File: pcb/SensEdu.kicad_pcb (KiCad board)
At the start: 4 copper layers, 99.1 x 54 mm, 147 parts, among them J1 Power, J10 Barrel_Jack_Switch, J11 Conn_01x04_Pin, J12 Conn_01x04_Pin, J13 Conn_02x01, J14 Conn_02x01, J15 Conn_02x01, J16 Conn_02x01, J19 Conn_03x01, J2 PWM, J20 Conn_01x04_Pin, J3 Analog, J4 PWM, J5 Analog, J6 Communication, J7 Digital, J9 Conn_01x04_Pin, U1 AD8426ACPZ-R7, U12 TLS850C2TE_V33, U13 NCP1117-2.5_SOT223, U2 AD8426ACPZ-R7, U3 LT1790ACS6-1.25, U4 ADA4891, U5 AD8426ACPZ-R7, U6 AD8426ACPZ-R7, U7 ADA4891, U8 DPS310XTSA1

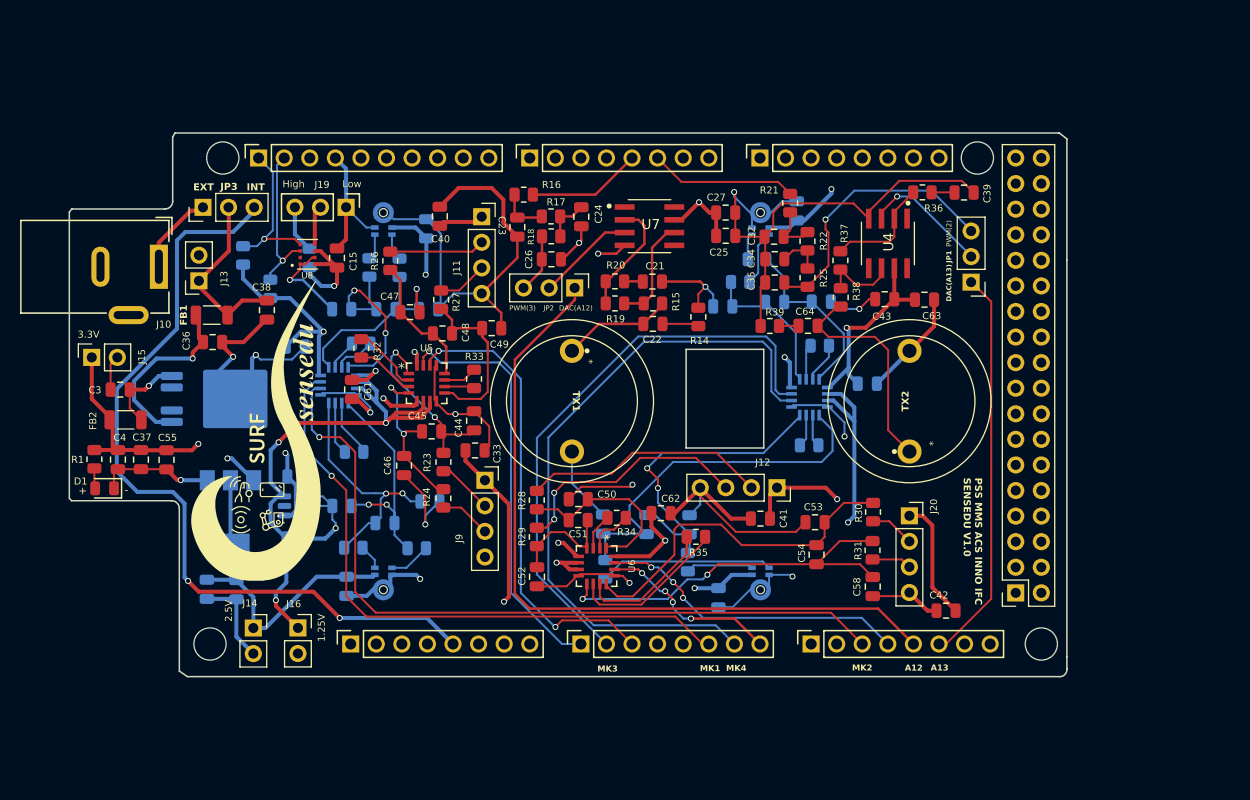
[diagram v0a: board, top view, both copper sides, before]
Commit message: pcb: New PCB revision (#88)
- Rearrange schematics
- Better symbols and footprints
- Better names and graphics
- Add simulations for DC offset after AC coupling
- Add BOM
- Redraw PCB layout
- Proper position for pressure and humidity sensor
- Better positions for EXT headers
- Silkscreen text labels for headers, pins, mics, etc.
- Change supply polarity and pin numbers of ADA4511
- Change cap of switches to 100n to reduce BOM
- Change supply of sensors to unison 3.3V
- Rearrange ADC pins
- Add digital switches instead of manual headers
- Add logos

---------

Co-authored-by: oberfeli <felix.ober@mailbox.org>
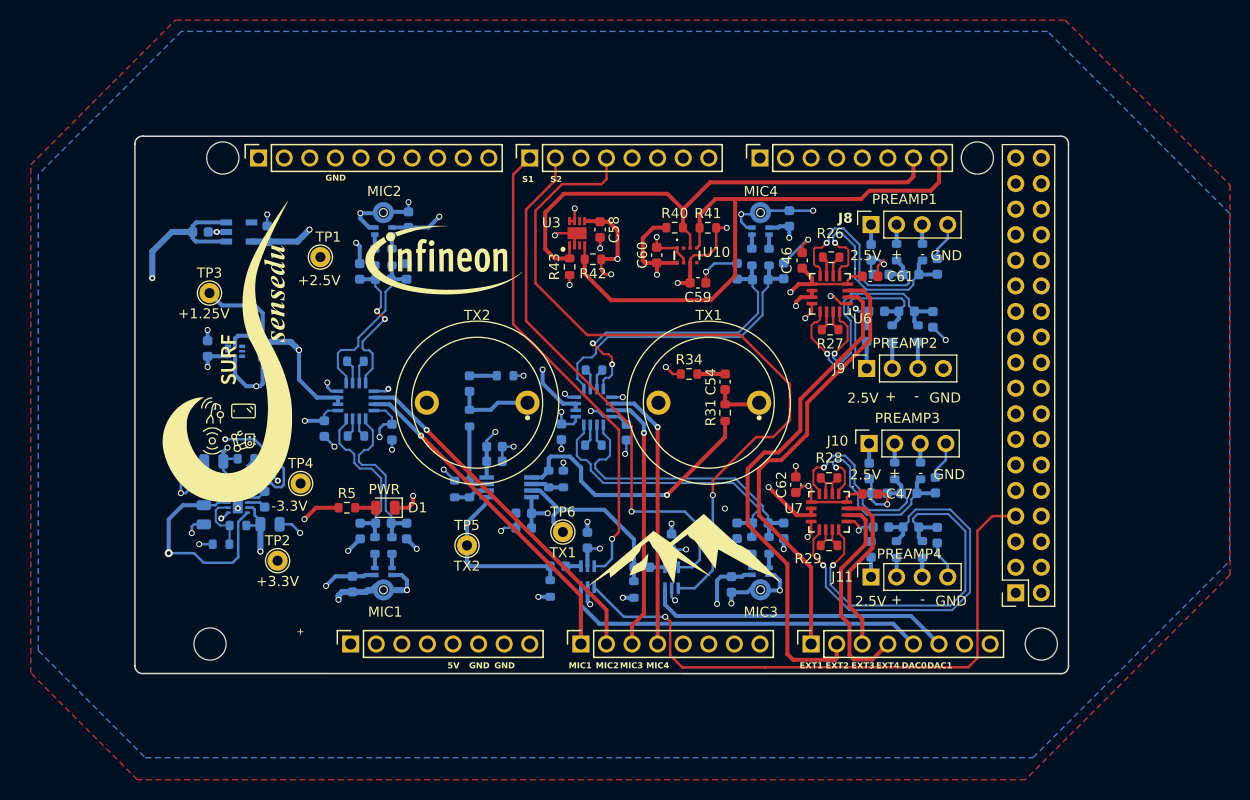
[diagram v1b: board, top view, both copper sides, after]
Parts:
- removed C63: 100n, Capacitor_SMD:C_0805_2012Metric
- removed C64: DNI, Capacitor_SMD:C_0805_2012Metric
- removed FB1, FB2: FerriteBead, Inductor_SMD:L_1206_3216Metric
- removed the G*** at (118.5, 76.2)
- removed J12, J20: Conn_01x04_Pin, Connector_PinSocket_2.54mm:PinSocket_1x04_P2.54mm_Vertical
- removed J13, J14, J15, J16: Conn_02x01, Connector_PinSocket_2.54mm:PinSocket_1x02_P2.54mm_Vertical
- removed J19: Conn_03x01, Connector_PinHeader_2.54mm:PinHeader_1x03_P2.54mm_Vertical
- removed the J9 at (141.3, 81.2)
- removed JP1, JP2, JP3: Jumper_3_Bridged12, Connector_PinHeader_2.54mm:PinHeader_1x03_P2.54mm_Vertical
- removed LS1, LS2: 328ST16M, SensEdu:328ST16M_Speaker
- removed U12: TLS850C2TE_V33, Package_TO_SOT_SMD:TO-252-4
- added C19: 100p, Capacitor_SMD:C_0603_1608Metric, B.Cu at (133.5, 60.5)
- added C59: 100n, Capacitor_SMD:C_0603_1608Metric, F.Cu at (162.4, 61.6)
- added C60: 100n, Capacitor_SMD:C_0603_1608Metric, F.Cu at (158.3, 58.8)
- added G***: LOGO, LOGO, F.Cu at (137.4, 59.4)
- added G***: LOGO, SensEdu:logo2, F.Cu at (115.7, 68.4)
- added G***: LOGO, LOGO, F.Cu at (161.1, 87.9)
- added J11: Conn_01x04_Pin, Connector_PinSocket_2.54mm:PinSocket_1x04_P2.54mm_Vertical, F.Cu at (179.6, 90.8)
- added J8: Conn_01x04_Pin, Connector_PinSocket_2.54mm:PinSocket_1x04_P2.54mm_Vertical, F.Cu at (179.6, 55.8)
- added R43: 10k, Resistor_SMD:R_0603_1608Metric, F.Cu at (149.7, 60.0)
- added TP1: +2.5V, TestPoint:TestPoint_THTPad_D2.0mm_Drill1.0mm, F.Cu at (124.9, 59.0)
- added TP2: +3.3V, TestPoint:TestPoint_THTPad_D2.0mm_Drill1.0mm, F.Cu at (120.7, 89.2)
- added TP3: +1.25V, TestPoint:TestPoint_THTPad_D2.0mm_Drill1.0mm, F.Cu at (113.9, 62.6)
- added TP4: -3.3V, TestPoint:TestPoint_THTPad_D2.0mm_Drill1.0mm, F.Cu at (123.0, 81.5)
- added TP5: TX2, TestPoint:TestPoint_THTPad_D2.0mm_Drill1.0mm, F.Cu at (139.5, 87.7)
- added TP6: TX1, TestPoint:TestPoint_THTPad_D2.0mm_Drill1.0mm, F.Cu at (149.0, 86.3)
- added TX1: 328ST16M, SensEdu:328ST16M_Speaker, F.Cu at (163.5, 73.5)
- added TX2: 328ST16M, SensEdu:328ST16M_Speaker, F.Cu at (140.5, 73.5)
- added U10: DPS368XTSA1, SensEdu:DPS368XTSA1, F.Cu at (161.3, 58.9)
- added U11: ADA4511-2ARMZ, SamacSys_Parts:SOP65P490X110-8N, B.Cu at (143.7, 81.9)
- added U9: NC7SB3157P6X, SensEdu:SOT65P210X110-6N, B.Cu at (151.5, 90.8)
- C1, C10, C11, C2: value 100n -> 1u; footprint Capacitor_SMD:C_0805_2012Metric -> Capacitor_SMD:C_0603_1608Metric
- C12, C13: value 470p -> 100n; footprint Capacitor_SMD:C_0805_2012Metric -> Capacitor_SMD:C_0603_1608Metric
- C14: value 1u -> 470p; footprint Capacitor_SMD:C_0805_2012Metric -> Capacitor_SMD:C_0603_1608Metric
- C15, C36: value 100n -> 470p; footprint Capacitor_SMD:C_0805_2012Metric -> Capacitor_SMD:C_0603_1608Metric; moved to B.Cu
- C16, C18, C57, C61, C62: footprint Capacitor_SMD:C_0805_2012Metric -> Capacitor_SMD:C_0603_1608Metric
- C17: value 470p -> 100p; footprint Capacitor_SMD:C_0805_2012Metric -> Capacitor_SMD:C_0603_1608Metric
- C20: value 1u -> 100n; footprint Capacitor_SMD:C_0805_2012Metric -> Capacitor_SMD:C_0603_1608Metric
- C21, C33, C44: footprint Capacitor_SMD:C_0805_2012Metric -> Capacitor_SMD:C_0603_1608Metric; moved to B.Cu
- C22: value DNI -> 470p; footprint Capacitor_SMD:C_0805_2012Metric -> Capacitor_SMD:C_0603_1608Metric; moved to B.Cu
- C23, C34, C35: value 1n -> 470p; footprint Capacitor_SMD:C_0805_2012Metric -> Capacitor_SMD:C_0603_1608Metric; moved to B.Cu
- C24, C26: value 1n -> 100p; footprint Capacitor_SMD:C_0805_2012Metric -> Capacitor_SMD:C_0603_1608Metric; moved to B.Cu
- C25, C39, C40, C41, C42: value 100n -> 100p; footprint Capacitor_SMD:C_0805_2012Metric -> Capacitor_SMD:C_0603_1608Metric; moved to B.Cu
- C27, C43: value 1u -> 100p; footprint Capacitor_SMD:C_0805_2012Metric -> Capacitor_SMD:C_0603_1608Metric; moved to B.Cu
- C28, C29, C46, C47: value 100p -> 1u; footprint Capacitor_SMD:C_0805_2012Metric -> Capacitor_SMD:C_0603_1608Metric
- C3: value 10u -> 1u; footprint Capacitor_SMD:C_0805_2012Metric -> Capacitor_SMD:C_0603_1608Metric; moved to B.Cu
- C30, C31, C58: value 100p -> 100n; footprint Capacitor_SMD:C_0805_2012Metric -> Capacitor_SMD:C_0603_1608Metric
- C32: value 1n -> 100n; footprint Capacitor_SMD:C_0805_2012Metric -> Capacitor_SMD:C_0603_1608Metric; moved to B.Cu
- C37: value 10u -> 470p; footprint Capacitor_SMD:C_0805_2012Metric -> Capacitor_SMD:C_0603_1608Metric; moved to B.Cu
- C38: value 10u -> 100p; footprint Capacitor_SMD:C_0805_2012Metric -> Capacitor_SMD:C_0603_1608Metric; moved to B.Cu
- C4: value 100n -> 1u; footprint Capacitor_SMD:C_0805_2012Metric -> Capacitor_SMD:C_0603_1608Metric; moved to B.Cu
- C45: value 470p -> 100p; footprint Capacitor_SMD:C_0805_2012Metric -> Capacitor_SMD:C_0603_1608Metric; moved to B.Cu
- C48, C51: value 470p -> 100n; footprint Capacitor_SMD:C_0805_2012Metric -> Capacitor_SMD:C_0603_1608Metric; moved to B.Cu
- C49, C52: value 100p -> 1u; footprint Capacitor_SMD:C_0805_2012Metric -> Capacitor_SMD:C_0603_1608Metric; moved to B.Cu
- C5: value 100p -> 4.7u
- C50, C53: value 100p -> 100n; footprint Capacitor_SMD:C_0805_2012Metric -> Capacitor_SMD:C_0603_1608Metric; moved to B.Cu
- C54: value 470p -> DNI; footprint Capacitor_SMD:C_0805_2012Metric -> Capacitor_SMD:C_0603_1608Metric
- C55: value 100n -> DNI; footprint Capacitor_SMD:C_0805_2012Metric -> Capacitor_SMD:C_0603_1608Metric; moved to B.Cu
- C56: value 10u -> 100n; footprint Capacitor_SMD:C_0805_2012Metric -> Capacitor_SMD:C_0603_1608Metric
- C6: value 470p -> 4.7u
- C7: value 1u -> 2.2u
- C8: value 100n -> 470n; footprint Capacitor_SMD:C_0805_2012Metric -> Capacitor_SMD:C_0603_1608Metric
- C9: value 100p -> 2.2u
- J10: value Barrel_Jack_Switch -> Conn_01x04_Pin; footprint Connector_BarrelJack:BarrelJack_Wuerth_6941xx301002 -> Connector_PinSocket_2.54mm:PinSocket_1x04_P2.54mm_Vertical
- R1: value 47 -> 130k; footprint Resistor_SMD:R_0805_2012Metric -> Resistor_SMD:R_0603_1608Metric; moved to B.Cu
- R10, R11, R6, R8, R9: footprint Resistor_SMD:R_0805_2012Metric -> Resistor_SMD:R_0603_1608Metric
- R12, R13, R7: value 1k -> 3.9k; footprint Resistor_SMD:R_0805_2012Metric -> Resistor_SMD:R_0603_1608Metric
- R14: value DNI -> 1k; footprint Resistor_SMD:R_0805_2012Metric -> Resistor_SMD:R_0603_1608Metric; moved to B.Cu
- R15: value 0 -> 1k; footprint Resistor_SMD:R_0805_2012Metric -> Resistor_SMD:R_0603_1608Metric; moved to B.Cu
- R16, R17: value 4.7k -> 1k; footprint Resistor_SMD:R_0805_2012Metric -> Resistor_SMD:R_0603_1608Metric; moved to B.Cu
- R18, R21, R22, R25: value 4.7k -> 3.9k; footprint Resistor_SMD:R_0805_2012Metric -> Resistor_SMD:R_0603_1608Metric; moved to B.Cu
- R19: value 3k -> 3.9k; footprint Resistor_SMD:R_0805_2012Metric -> Resistor_SMD:R_0603_1608Metric; moved to B.Cu
- R2: value 1k -> 75k; footprint Resistor_SMD:R_0805_2012Metric -> Resistor_SMD:R_0603_1608Metric
- R20: value 1k -> 3.9k; footprint Resistor_SMD:R_0805_2012Metric -> Resistor_SMD:R_0603_1608Metric; moved to B.Cu
- R23, R24: footprint Resistor_SMD:R_0805_2012Metric -> Resistor_SMD:R_0603_1608Metric; moved to B.Cu
- R26, R27, R28, R29: value 3.9k -> 1k; footprint Resistor_SMD:R_0805_2012Metric -> Resistor_SMD:R_0603_1608Metric
- R3: value 3.9k -> 130k; footprint Resistor_SMD:R_0805_2012Metric -> Resistor_SMD:R_0603_1608Metric
- R30: value 3.9k -> 1.2k; footprint Resistor_SMD:R_0805_2012Metric -> Resistor_SMD:R_0603_1608Metric; moved to B.Cu
- R31: value 3.9k -> 0; footprint Resistor_SMD:R_0805_2012Metric -> Resistor_SMD:R_0603_1608Metric
- R32, R33, R36: value 1k -> 22k; footprint Resistor_SMD:R_0805_2012Metric -> Resistor_SMD:R_0603_1608Metric; moved to B.Cu
- R34: value 1k -> DNI; footprint Resistor_SMD:R_0805_2012Metric -> Resistor_SMD:R_0603_1608Metric
- R35: value 1k -> 0; footprint Resistor_SMD:R_0805_2012Metric -> Resistor_SMD:R_0603_1608Metric; moved to B.Cu
- R37: value 3k -> DNI; footprint Resistor_SMD:R_0805_2012Metric -> Resistor_SMD:R_0603_1608Metric; moved to B.Cu
- R38: value 0 -> 22k; footprint Resistor_SMD:R_0805_2012Metric -> Resistor_SMD:R_0603_1608Metric; moved to B.Cu
- R39: value DNI -> 1.2k; footprint Resistor_SMD:R_0805_2012Metric -> Resistor_SMD:R_0603_1608Metric; moved to B.Cu
- R4: value 3.9k -> 75k; footprint Resistor_SMD:R_0805_2012Metric -> Resistor_SMD:R_0603_1608Metric
- R40, R41, R42: footprint Resistor_SMD:R_0805_2012Metric -> Resistor_SMD:R_0603_1608Metric; moved to F.Cu
- R5: value 3.9k -> 47; footprint Resistor_SMD:R_0805_2012Metric -> Resistor_SMD:R_0603_1608Metric; moved to F.Cu
- U1: value AD8426ACPZ-R7 -> LDLN025M25R; footprint SensEdu:QFN65P400X400X100-16N -> SamacSys_Parts:SOT95P280X145-5N
- U13: value NCP1117-2.5_SOT223 -> TS3312AQPR; footprint Package_TO_SOT_SMD:SOT-223-3_TabPin2 -> SamacSys_Parts:TS3312AQPR
- U2: value AD8426ACPZ-R7 -> LM27762DSST; footprint SensEdu:QFN65P400X400X100-16N -> SensEdu:IC_LM27762DSST
- U3: value LT1790ACS6-1.25 -> SHT35-DIS-B2.5KS; footprint Package_TO_SOT_SMD:TSOT-23-6 -> SensEdu:SHT35-DIS-B2.5KS; moved to F.Cu
- U4: value ADA4891 -> AD8426ACPZ-R7; footprint SensEdu:ADA4891-1ARZ -> SensEdu:QFN65P400X400X100-16N; moved to B.Cu
- U5: moved to B.Cu
- U7: value ADA4891 -> AD8426ACPZ-R7; footprint SensEdu:ADA4891-1ARZ -> SensEdu:QFN65P400X400X100-16N
- U8: value DPS310XTSA1 -> NC7SB3157P6X; footprint SensEdu:XDCR_DPS310XTSA1 -> SensEdu:SOT65P210X110-6N; moved to B.Cu
- moved C37 78.6 mm to (183.6, 60.8), turned to 0 degrees
- moved J10 72.7 mm to (179.4, 77.5), turned to 90 degrees
- moved C36 70.8 mm to (183.4, 82.5)
- moved C38 66.1 mm to (185.8, 65.2), turned to 90 degrees
- moved C2 63.0 mm to (113.0, 56.5), turned to 0 degrees
- moved C9 62.4 mm to (114.3, 79.3), turned to 0 degrees
- moved C6 60.5 mm to (113.3, 84.6), turned to -90 degrees
- moved C40 58.7 mm to (186.2, 86.7)
- moved U2 57.7 mm to (116.7, 83.2), turned to 0 degrees
- moved U4 55.1 mm to (128.5, 73.3), turned to 90 degrees
- moved R36 55.0 mm to (138.3, 82.1), turned to -90 degrees
- moved C5 54.4 mm to (113.4, 81.6), turned to 180 degrees
- moved C61 52.7 mm to (179.5, 61.0), turned to 0 degrees
- moved C31 52.2 mm to (179.2, 66.6), turned to 90 degrees
- moved C3 50.4 mm to (155.3, 76.4), turned to -90 degrees
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- renumbered J11 to J9, MK4 to MK3, MK3 to MK4
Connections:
- net /37 renamed SE_PWM_2
- C1 pad 1: +2.5V -> +3.3V
- C10 pad 1: +2.5V -> +3.3V
- C11 pad 1: +2.5V -> GND
- C11 pad 2: GND -> +1.25V_REF
- C12 pad 1: /Microphones/mic2_out1 -> +2.5V
- C12 pad 2: /Microphones/mic2_out2 -> GND
- C13 pad 1: /Microphones/mic1_out1 -> +2.5V
- C13 pad 2: /Microphones/mic1_out2 -> GND
- C14 pad 1: +3.3V -> mic1_out_P
- C14 pad 2: GND -> mic1_out_N
- C15 pad 1: +3.3V -> mic2_out_P
- C15 pad 2: GND -> mic2_out_N
- C16 pad 2: /Microphones/mic4_out1 -> mic1_out_N
- C17 pad 1: /Microphones/mic4_out1 -> GND
- C17 pad 2: /Microphones/mic4_out2 -> mic1_out_P
- C18 pad 2: /Microphones/mic4_out2 -> mic2_out_N
- C2 pad 1: +2.5V -> /3V3_INO
- C20 pad 1: +3.3V -> +2.5V
- C21 pad 1: Net-(C21-Pad1) -> +2.5V
- C22 pad 1: Net-(C22-Pad1) -> mic3_out_P
- C22 pad 2: Net-(C22-Pad2) -> mic3_out_N
- C23 pad 1: Net-(C23-Pad1) -> mic4_out_P
- C23 pad 2: GND -> mic4_out_N
- C24 pad 1: Net-(C24-Pad1) -> GND
- C24 pad 2: GND -> mic3_out_N
- C25 pad 2: +3.3V -> mic3_out_P
- C26 pad 1: Net-(JP2-B) -> GND
- C26 pad 2: GND -> mic4_out_N
- C27 pad 2: +3.3V -> mic4_out_P
- C28 pad 1: GND -> +3.3V
- C28 pad 2: /Microphones/mic2_out1 -> GND
- C29 pad 1: GND -> +3.3V
- C29 pad 2: /Microphones/mic2_out2 -> GND
- C3 pad 1: Net-(U12-Q) -> +3.3V
- C30 pad 1: GND -> +2.5V
- C30 pad 2: /Microphones/mic1_out1 -> GND
- C31 pad 1: GND -> +2.5V
- C31 pad 2: /Microphones/mic1_out2 -> GND
- C32 pad 1: Net-(C32-Pad1) -> +2.5V
- C34 pad 1: Net-(C34-Pad1) -> amp2_out_P
- C34 pad 2: GND -> amp2_out_N
- C35 pad 1: Net-(JP1-B) -> amp4_out_P
- C35 pad 2: GND -> amp4_out_N
- C36 pad 1: Net-(U12-I) -> amp3_out_P
- C36 pad 2: GND -> amp3_out_N
- C37 pad 1: +3.3V -> amp1_out_P
- C37 pad 2: GND -> amp1_out_N
- C38 pad 1: Net-(J13-Pin_1) -> GND
- C38 pad 2: GND -> amp2_out_N
- C39 pad 1: Net-(C39-Pad1) -> GND
- C39 pad 2: GND -> amp2_out_P
- C4 pad 1: +3.3V -> +2.5V
- C40 pad 1: +2.5V -> GND
- C40 pad 2: GND -> amp4_out_N
- C41 pad 1: +2.5V -> GND
- C41 pad 2: GND -> amp4_out_P
- C42 pad 1: +2.5V -> GND
- C42 pad 2: GND -> amp3_out_N
- C43 pad 2: +3.3V -> amp3_out_P
- C44 pad 2: /Microphones/External Microphone Connectors/mic5_out1 -> amp1_out_N
- C45 pad 1: /Microphones/External Microphone Connectors/mic5_out1 -> GND
- C45 pad 2: /Microphones/External Microphone Connectors/mic5_out2 -> amp1_out_P
- C46 pad 1: GND -> +3.3V
- C46 pad 2: /Microphones/External Microphone Connectors/mic5_out2 -> GND
- C47 pad 1: GND -> +3.3V
- C47 pad 2: /Microphones/External Microphone Connectors/mic6_out1 -> GND
- C48 pad 1: /Microphones/External Microphone Connectors/mic6_out1 -> GND
- C48 pad 2: /Microphones/External Microphone Connectors/mic6_out2 -> +3.3V
- C49 pad 1: GND -> -3V3
- C49 pad 2: /Microphones/External Microphone Connectors/mic6_out2 -> GND
- C5 pad 1: GND -> /Power/CP
- C5 pad 2: /Microphones/mic3_out1 -> GND
- C50 pad 1: GND -> -3V3
- C50 pad 2: /Microphones/External Microphone Connectors/mic7_out1 -> GND
- C51 pad 1: /Microphones/External Microphone Connectors/mic7_out1 -> GND
- C51 pad 2: /Microphones/External Microphone Connectors/mic7_out2 -> +3.3V
- C52 pad 1: GND -> +3.3V
- C52 pad 2: /Microphones/External Microphone Connectors/mic7_out2 -> GND
- C53 pad 1: GND -> /Speakers/SW1_OUT
- C53 pad 2: /Microphones/External Microphone Connectors/mic8_out1 -> /Speakers/+IN_CH1
- C54 pad 1: /Microphones/External Microphone Connectors/mic8_out1 -> /Speakers/TX1
- C54 pad 2: /Microphones/External Microphone Connectors/mic8_out2 -> Net-(C54-Pad2)
- C55 pad 1: +3.3V -> /Speakers/TX2
- C55 pad 2: GND -> Net-(C55-Pad2)
- C56 pad 1: +2.5V -> GND
- C56 pad 2: GND -> +3.3V
- C57 pad 1: +2.5V -> /Speakers/SW2_OUT
- C57 pad 2: GND -> /Speakers/+IN_CH2
- C58 pad 2: /Microphones/External Microphone Connectors/mic8_out2 -> +3.3V
- C6 pad 1: /Microphones/mic3_out1 -> /+5V_ARDUINO
- C6 pad 2: /Microphones/mic3_out2 -> GND
- C7 pad 1: GND -> +3.3V
- C7 pad 2: +1.25V_REF -> GND
- C8 pad 1: +3.3V -> Net-(U2-C1+)
- C8 pad 2: GND -> Net-(U2-C1-)
- C9 pad 2: /Microphones/mic3_out2 -> -3V3
- D1 pad 2: Net-(D1-A) -> /Power/LED+
- J1 pad 4: /3V3 -> /3V3_INO
- J1 pad 5: /5V0 -> /+5V_ARDUINO
- J10 pad 1: Net-(JP3-A) -> +2.5V
- J10 pad 2: GND -> Net-(J10-Pin_2)
- J10 pad 3: unconnected-(J10-Pad3) -> Net-(J10-Pin_3)
- J3 pad 1: /A0 -> /MIC1_OUT
- J3 pad 2: /A1 -> /MIC2_OUT
- J3 pad 3: /A2 -> /MIC3_OUT
- J3 pad 4: /A3 -> /MIC4_OUT
- J3 pad 6: /A5 -> unconnected-(J3-Pin_6-Pad6)
- J3 pad 7: /A6 -> unconnected-(J3-Pin_7-Pad7)
- J3 pad 8: /A7 -> unconnected-(J3-Pin_8-Pad8)
- J4 pad 1: /*7 -> S2
- J4 pad 2: /*6 -> S1
- J4 pad 4: /*4 -> SE_PWM_1
- J4 pad 5: /*3 -> /4*
- J4 pad 6: /*2 -> /3*
- J5 pad 1: /A8 -> /AMP1_OUT
- J5 pad 2: /A9 -> /AMP2_OUT
- J5 pad 3: /A10 -> /AMP3_OUT
- J5 pad 4: /Microphones/MIC7_OUT -> /AMP4_OUT
- J5 pad 5: A12 -> DAC0
- J5 pad 6: A13 -> DAC1
- J6 pad 7: /SDA/20 -> /SDA
- J6 pad 8: /SCL/21 -> /SCL
- J7 pad 7: /48 -> SE_PWM_3
- J9 pad 2: Net-(J11-Pin_2) -> Net-(J9-Pin_2)
- J9 pad 3: Net-(J11-Pin_3) -> Net-(J9-Pin_3)
- MK3 pad 1: Net-(MK4-OUTPUT+) -> Net-(MK3-OUTPUT+)
- MK3 pad 3: Net-(MK4-OUTPUT-) -> Net-(MK3-OUTPUT-)
- MK4 pad 1: Net-(MK3-OUTPUT+) -> Net-(MK4-OUTPUT+)
- MK4 pad 3: Net-(MK3-OUTPUT-) -> Net-(MK4-OUTPUT-)
- R1 pad 2: Net-(D1-A) -> /Power/FB+
- R10 pad 1: Net-(MK4-OUTPUT+) -> Net-(MK3-OUTPUT-)
- R10 pad 2: /Microphones/mic4_out1 -> mic3_out_N
- R11 pad 1: Net-(MK4-OUTPUT-) -> Net-(MK3-OUTPUT+)
- R11 pad 2: /Microphones/mic4_out2 -> mic3_out_P
- R12 pad 1: Net-(U2-RG1_2) -> Net-(MK4-OUTPUT-)
- R12 pad 2: Net-(U2-RG1) -> mic4_out_N
- R13 pad 1: Net-(U2-RG2_2) -> Net-(MK4-OUTPUT+)
- R13 pad 2: Net-(U2-RG2) -> mic4_out_P
- R14 pad 1: GND -> Net-(U4-RG1_2)
- R14 pad 2: Net-(C22-Pad2) -> Net-(U4-RG1)
- R15 pad 1: Net-(U7-OUT) -> Net-(U4-RG2_2)
- R15 pad 2: Net-(C22-Pad1) -> Net-(U4-RG2)
- R16 pad 1: Net-(C23-Pad1) -> Net-(U5-RG1_2)
- R16 pad 2: /*3 -> Net-(U5-RG1)
- R17 pad 1: Net-(C23-Pad1) -> Net-(U5-RG2_2)
- R17 pad 2: Net-(C24-Pad1) -> Net-(U5-RG2)
- R18 pad 1: Net-(C24-Pad1) -> Net-(J8-Pin_3)
- R18 pad 2: Net-(JP2-B) -> amp1_out_N
- R19 pad 1: Net-(U7--IN) -> Net-(J8-Pin_2)
- R19 pad 2: Net-(U7-OUT) -> amp1_out_P
- R2 pad 1: Net-(U1-RG1_2) -> /Power/FB+
- R2 pad 2: Net-(U1-RG1) -> GND
- R20 pad 1: Net-(U7--IN) -> Net-(J9-Pin_3)
- R20 pad 2: Net-(C21-Pad1) -> amp2_out_N
- R21 pad 1: Net-(C32-Pad1) -> Net-(J9-Pin_2)
- R21 pad 2: /*2 -> amp2_out_P
- R22 pad 1: Net-(C32-Pad1) -> Net-(J10-Pin_3)
- R22 pad 2: Net-(C34-Pad1) -> amp3_out_N
- R23 pad 1: Net-(J9-Pin_2) -> Net-(J10-Pin_2)
- R23 pad 2: /Microphones/External Microphone Connectors/mic5_out1 -> amp3_out_P
- R24 pad 1: Net-(J9-Pin_3) -> /Microphones/External Microphone Connectors/out-
- R24 pad 2: /Microphones/External Microphone Connectors/mic5_out2 -> amp4_out_N
- R25 pad 1: Net-(C34-Pad1) -> /Microphones/External Microphone Connectors/out+
- R25 pad 2: Net-(JP1-B) -> amp4_out_P
- R26 pad 1: Net-(J11-Pin_2) -> Net-(U6-RG1_2)
- R26 pad 2: /Microphones/External Microphone Connectors/mic6_out1 -> Net-(U6-RG1)
- R27 pad 1: Net-(J11-Pin_3) -> Net-(U6-RG2_2)
- R27 pad 2: /Microphones/External Microphone Connectors/mic6_out2 -> Net-(U6-RG2)
- R28 pad 1: Net-(J12-Pin_2) -> Net-(U7-RG1_2)
- R28 pad 2: /Microphones/External Microphone Connectors/mic7_out1 -> Net-(U7-RG1)
- R29 pad 1: Net-(J12-Pin_3) -> Net-(U7-RG2_2)
- R29 pad 2: /Microphones/External Microphone Connectors/mic7_out2 -> Net-(U7-RG2)
- R3 pad 1: Net-(MK2-OUTPUT+) -> GND
- R3 pad 2: /Microphones/mic2_out1 -> /Power/FB-
- R30 pad 1: Net-(J20-Pin_2) -> GND
- R30 pad 2: /Microphones/External Microphone Connectors/mic8_out1 -> /Speakers/+IN_CH1
- R31 pad 1: Net-(J20-Pin_3) -> /Speakers/TX1_IN
- R31 pad 2: /Microphones/External Microphone Connectors/mic8_out2 -> /Speakers/TX1
- R32 pad 1: Net-(U5-RG1_2) -> GND
- R32 pad 2: Net-(U5-RG1) -> /Speakers/-IN_CH1
- R33 pad 1: Net-(U5-RG2_2) -> /Speakers/-IN_CH1
- R33 pad 2: Net-(U5-RG2) -> /Speakers/TX1_IN
- R34 pad 1: Net-(U6-RG1_2) -> GND
- R34 pad 2: Net-(U6-RG1) -> Net-(C54-Pad2)
- R35 pad 1: Net-(U6-RG2_2) -> /Speakers/TX2_IN
- R35 pad 2: Net-(U6-RG2) -> /Speakers/TX2
- R36 pad 1: Net-(U4--IN) -> GND
- R36 pad 2: Net-(C39-Pad1) -> /Speakers/-IN_CH2
- R37 pad 1: Net-(U4--IN) -> GND
- R37 pad 2: Net-(U4-OUT) -> Net-(C55-Pad2)
- R38 pad 1: Net-(U4-OUT) -> /Speakers/-IN_CH2
- R38 pad 2: Net-(C64-Pad1) -> /Speakers/TX2_IN
- R39 pad 2: Net-(C64-Pad2) -> /Speakers/+IN_CH2
- R4 pad 1: Net-(MK1-OUTPUT+) -> /Power/FB-
- R4 pad 2: /Microphones/mic1_out1 -> -3V3
- R40 pad 1: /SCL1 -> +3.3V
- R40 pad 2: +3.3V -> /SDA
- R41 pad 1: +3.3V -> /SCL
- R41 pad 2: /SDA1 -> +3.3V
- R42 pad 1: Net-(J19-B) -> +3.3V
- R42 pad 2: +3.3V -> /SCL
- R5 pad 1: Net-(MK1-OUTPUT-) -> +3.3V
- R5 pad 2: /Microphones/mic1_out2 -> /Power/LED+
- R6 pad 1: Net-(MK2-OUTPUT-) -> Net-(MK1-OUTPUT-)
- R6 pad 2: /Microphones/mic2_out2 -> mic1_out_N
- R7 pad 1: Net-(U1-RG2_2) -> Net-(MK1-OUTPUT+)
- R7 pad 2: Net-(U1-RG2) -> mic1_out_P
- R8 pad 1: Net-(MK3-OUTPUT+) -> Net-(MK2-OUTPUT-)
- R8 pad 2: /Microphones/mic3_out1 -> mic2_out_N
- R9 pad 1: Net-(MK3-OUTPUT-) -> Net-(MK2-OUTPUT+)
- R9 pad 2: /Microphones/mic3_out2 -> mic2_out_P
- U1 pad 1: /Microphones/mic1_out1 -> /3V3_INO
- U1 pad 2: Net-(U1-RG1_2) -> GND
- U1 pad 3: Net-(U1-RG1) -> /3V3_INO
- U1 pad 4: /Microphones/mic1_out2 -> unconnected-(U1-NC-Pad4)
- U1 pad 5: +3.3V -> +2.5V
- U13 pad 1: GND -> unconnected-(U13-NC_1-Pad1)
- U13 pad 2: +2.5V -> unconnected-(U13-NC_2-Pad2)
- U13 pad 3: +3.3V -> unconnected-(U13-NC_3-Pad3)
- U2 pad 1: /Microphones/mic3_out1 -> GND
- U2 pad 10: Net-(U2-RG2_2) -> Net-(U2-C1+)
- U2 pad 11: Net-(U2-RG2) -> +3.3V
- U2 pad 12: /Microphones/mic4_out1 -> /+5V_ARDUINO
- U2 pad 2: Net-(U2-RG1_2) -> /Power/FB+
- U2 pad 3: Net-(U2-RG1) -> /+5V_ARDUINO
- U2 pad 4: /Microphones/mic3_out2 -> GND
- U2 pad 5: +3.3V -> /Power/CP
- U2 pad 6: +1.25V_REF -> -3V3
- U2 pad 7: +1.25V_REF -> /Power/FB-
- U2 pad 8: GND -> /+5V_ARDUINO
- U2 pad 9: /Microphones/mic4_out2 -> Net-(U2-C1-)
- U3 pad 1: GND -> /SDA
- U3 pad 4: +3.3V -> /SCL
- U3 pad 5: unconnected-(U3-DNC-Pad5) -> +3.3V
- U3 pad 6: +1.25V_REF -> unconnected-(U3-NRESET-Pad6)
- U4 pad 1: unconnected-(U4-NC_1-Pad1) -> mic1_out_N
- U4 pad 2: Net-(U4--IN) -> Net-(U4-RG1_2)
- U4 pad 3: Net-(JP1-C) -> Net-(U4-RG1)
- U4 pad 4: GND -> mic1_out_P
- U4 pad 5: unconnected-(U4-NC_2-Pad5) -> +3.3V
- U4 pad 6: Net-(U4-OUT) -> +1.25V_REF
- U4 pad 7: +3.3V -> +1.25V_REF
- U4 pad 8: unconnected-(U4-NC_3-Pad8) -> GND
- U5 pad 1: /Microphones/External Microphone Connectors/mic5_out1 -> mic3_out_N
- U5 pad 12: /Microphones/External Microphone Connectors/mic6_out1 -> mic4_out_N
- U5 pad 14: /A2 -> /MIC4_OUT
- U5 pad 15: /A0 -> /MIC3_OUT
- U5 pad 4: /Microphones/External Microphone Connectors/mic5_out2 -> mic3_out_P
- U5 pad 9: /Microphones/External Microphone Connectors/mic6_out2 -> mic4_out_P
- U6 pad 1: /Microphones/External Microphone Connectors/mic7_out1 -> amp1_out_N
- U6 pad 12: /Microphones/External Microphone Connectors/mic8_out1 -> amp2_out_N
- U6 pad 14: /A7 -> /AMP2_OUT
- U6 pad 15: /Microphones/MIC7_OUT -> /AMP1_OUT
- U6 pad 4: /Microphones/External Microphone Connectors/mic7_out2 -> amp1_out_P
- U6 pad 9: /Microphones/External Microphone Connectors/mic8_out2 -> amp2_out_P
- U7 pad 1: unconnected-(U7-NC_1-Pad1) -> amp3_out_N
- U7 pad 2: Net-(U7--IN) -> Net-(U7-RG1_2)
- U7 pad 3: Net-(JP2-C) -> Net-(U7-RG1)
- U7 pad 4: GND -> amp3_out_P
- U7 pad 5: unconnected-(U7-NC_2-Pad5) -> +3.3V
- U7 pad 6: Net-(U7-OUT) -> +1.25V_REF
- U7 pad 7: +3.3V -> +1.25V_REF
- U7 pad 8: unconnected-(U7-NC_3-Pad8) -> GND
- U8 pad 1: GND -> SE_PWM_1
- U8 pad 2: unconnected-(U8-~{CSB}-Pad2) -> GND
- U8 pad 3: /SDA1 -> DAC1
- U8 pad 4: /SCL1 -> /Speakers/SW1_OUT
- U8 pad 5: Net-(J19-C) -> +3.3V
- U8 pad 6: +3.3V -> S1
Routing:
- net GND: track 320.6 -> 156.9 mm, vias 19 -> 60
- net +2.5V: track 190.7 -> 34.6 mm
- net +3.3V: track 228.4 -> 90.9 mm, vias 13 -> 18
- net /+5V_ARDUINO: track 0.00 -> 83.0 mm, vias 0 -> 2
- net /5V0: track 79.1 -> 0.00 mm, vias 2 -> 0
- net /A10: track 76.3 -> 0.00 mm, vias 1 -> 0
- net /3V3_INO: track 0.00 -> 74.5 mm, vias 0 -> 1
- net A12: track 74.4 -> 0.00 mm
- net SE_PWM_1: track 0.00 -> 73.8 mm, vias 0 -> 1
- net /A6: track 68.0 -> 0.00 mm
- net /A5: track 61.8 -> 0.00 mm, vias 1 -> 0
- net SE_PWM_3: track 0.00 -> 60.7 mm, vias 0 -> 1
- net /SCL: track 0.00 -> 58.5 mm
- net /A1: track 57.6 -> 0.00 mm
- net S1: track 0.00 -> 53.8 mm, vias 0 -> 1
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- added copper zone on B.Cu, net GND
- added copper zone on F.Cu, net GND
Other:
- board size 99.1 x 54 mm -> 92.7 x 53.4 mm
- board text added: "+"
- board text added: "-"
- board text added: "."
- board text added: "10.39394 mm is the wavelength of 33khz sound wave in air at 20 degrees nlambda/2 is the spacing"
- board text added: "2.5V"
- board text added: "3.3V -> 2.5V"
- board text added: "5V"
- board text added: "5V -> +/-3.3V"
- board text added: "DAC0"
- board text added: "DAC1"
- board text added: "EXT1"
- board text added: "EXT2"
- board text added: "EXT3"
- board text added: "EXT4"
- board text added: "GND"
- board text added: "MIC1"
- board text added: "MIC2"
- board text added: "MIC3"
- board text added: "MIC4"
- board text added: "PREAMP1"
- board text added: "PREAMP2"
- board text added: "PREAMP3"
- board text added: "PREAMP4"
- board text added: "PWR"
- board text added: "S1"
- board text added: "S2"
- board text removed: "A12"
- board text removed: "A13"
- board text removed: "DAC(A12)"
- board text removed: "DAC(A13)"
- board text removed: "EXT"
- board text removed: "INT"
- board text removed: "MK2"
- board text removed: "MK3"
- board text removed: "MK4"
- board text removed: "PSS MMS ACS INNO IFC SENSEDU V1.0"
- board text removed: "PWM(2)"
- board text removed: "PWM(3)"

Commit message: feat: Prepare 0.9 PCB with fixed issues from 0.8 tests (#102)
* feat: Upgrade speaker simulation to realistic one

* feat: Improve PCB design after tests of rev 0.8

- Added new generation of humidity sensor
- New silkscreen information for different components
- Added additional testpoints
- Removed PWM path for ultrasound transmitter

* refactor: cleanup of symbol and footprint library

- removed components that are not used anymore
- ran final DRC to prepare for manufacturing

* feat: Update BOM with extra res, caps, tps and sht

* fix: Rename schematics to match the docs
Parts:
- removed C61, C62: 1u, Capacitor_SMD:C_0603_1608Metric
- removed U11: ADA4511-2ARMZ, SamacSys_Parts:SOP65P490X110-8N
- removed U13: TS3312AQPR, SamacSys_Parts:TS3312AQPR
- added TP10: DAC0, SensEdu:TestPoint_THTPad_D2.0mm_Drill1.0mm, F.Cu at (152.4, 88.4)
- added TP7: DAC1, SensEdu:TestPoint_THTPad_D2.0mm_Drill1.0mm, F.Cu at (143.8, 88.4)
- added TP8: TX1, SensEdu:TestPoint_THTPad_D2.0mm_Drill1.0mm, F.Cu at (171.7, 66.3)
- added TP9: TX2, SensEdu:TestPoint_THTPad_D2.0mm_Drill1.0mm, F.Cu at (148.8, 66.3)
- C1, C16, C17, C2, C24, C25, C28, C29, C30, C31, C32, C33, C34, C35, C36, C37, C38, C39, C40, C41, C42, C43, C44, C45, C46, C47, C53, C55, C58, C59, C60: footprint Capacitor_SMD:C_0603_1608Metric -> SensEdu:C_0603_1608Metric
- C10, C11, C52: value 1u -> 100n; footprint Capacitor_SMD:C_0603_1608Metric -> SensEdu:C_0603_1608Metric
- C12, C13, C20, C21: value 100n -> 470p; footprint Capacitor_SMD:C_0603_1608Metric -> SensEdu:C_0603_1608Metric
- C14, C15, C22, C23: value 470p -> 100p; footprint Capacitor_SMD:C_0603_1608Metric -> SensEdu:C_0603_1608Metric
- C18, C19: value 100p -> 100n; footprint Capacitor_SMD:C_0603_1608Metric -> SensEdu:C_0603_1608Metric
- C26, C27: value 100p -> 1u; footprint Capacitor_SMD:C_0603_1608Metric -> SensEdu:C_0603_1608Metric
- C3, C4: value 1u -> 4.7u; footprint Capacitor_SMD:C_0603_1608Metric -> SensEdu:C_0805_2012Metric
- C48: value 100n -> 1u; footprint Capacitor_SMD:C_0603_1608Metric -> SensEdu:C_0603_1608Metric; moved to F.Cu
- C49: footprint Capacitor_SMD:C_0603_1608Metric -> SensEdu:C_0603_1608Metric; moved to F.Cu
- C5: value 4.7u -> 2.2u; footprint Capacitor_SMD:C_0805_2012Metric -> SensEdu:C_0805_2012Metric
- C50, C57: value 100n -> 1n; footprint Capacitor_SMD:C_0603_1608Metric -> SensEdu:C_0603_1608Metric
- C51: value 100n -> 1u; footprint Capacitor_SMD:C_0603_1608Metric -> SensEdu:C_0603_1608Metric
- C54: value DNI -> 1u; footprint Capacitor_SMD:C_0603_1608Metric -> SensEdu:C_0603_1608Metric; moved to B.Cu
- C56: value 100n -> DNI; footprint Capacitor_SMD:C_0603_1608Metric -> SensEdu:C_0603_1608Metric
- C6: value 4.7u -> 470n; footprint Capacitor_SMD:C_0805_2012Metric -> SensEdu:C_0603_1608Metric
- C7: footprint Capacitor_SMD:C_0805_2012Metric -> SensEdu:C_0805_2012Metric
- C8: value 470n -> 1u; footprint Capacitor_SMD:C_0603_1608Metric -> SensEdu:C_0603_1608Metric
- C9: value 2.2u -> 1u; footprint Capacitor_SMD:C_0805_2012Metric -> SensEdu:C_0603_1608Metric
- D1: footprint LED_SMD:LED_0805_2012Metric -> SensEdu:LED_0805_2012Metric
- G***: footprint LOGO -> SensEdu:LOGO
- J1, J3, J4, J5, J6: footprint Connector_PinSocket_2.54mm:PinSocket_1x08_P2.54mm_Vertical -> SensEdu:PinSocket_1x08_P2.54mm_Vertical
- J10, J11, J8, J9: footprint Connector_PinSocket_2.54mm:PinSocket_1x04_P2.54mm_Vertical -> SensEdu:PinSocket_1x04_P2.54mm_Vertical
- J2: footprint Connector_PinSocket_2.54mm:PinSocket_1x10_P2.54mm_Vertical -> SensEdu:PinSocket_1x10_P2.54mm_Vertical
- J7: footprint Connector_PinSocket_2.54mm:PinSocket_2x18_P2.54mm_Vertical -> SensEdu:PinSocket_2x18_P2.54mm_Vertical
- MH1, MH2, MH5, MH6: footprint Arduino_MountingHole:MountingHole_3.2mm -> SensEdu:MountingHole_3.2mm
- R1, R10, R11, R12, R13, R14, R15, R16, R17, R18, R19, R2, R20, R21, R22, R23, R24, R25, R26, R27, R28, R29, R32, R33, R36, R37, R38, R40, R41, R42, R43, R5, R6, R7, R8, R9: footprint Resistor_SMD:R_0603_1608Metric -> SensEdu:R_0603_1608Metric
- R3: value 130k -> 75k; footprint Resistor_SMD:R_0603_1608Metric -> SensEdu:R_0603_1608Metric
- R30, R39: value 1.2k -> 43k; footprint Resistor_SMD:R_0603_1608Metric -> SensEdu:R_0603_1608Metric
- R31: value 0 -> 100; footprint Resistor_SMD:R_0603_1608Metric -> SensEdu:R_0603_1608Metric; moved to B.Cu
- R34: footprint Resistor_SMD:R_0603_1608Metric -> SensEdu:R_0603_1608Metric; moved to B.Cu
- R35: value 0 -> 100; footprint Resistor_SMD:R_0603_1608Metric -> SensEdu:R_0603_1608Metric
- R4: value 75k -> 130k; footprint Resistor_SMD:R_0603_1608Metric -> SensEdu:R_0603_1608Metric
- TP1, TP2: footprint TestPoint:TestPoint_THTPad_D2.0mm_Drill1.0mm -> SensEdu:TestPoint_THTPad_D2.0mm_Drill1.0mm
- TP3: value +1.25V -> 5018; footprint TestPoint:TestPoint_THTPad_D2.0mm_Drill1.0mm -> SensEdu:5018
- TP4: value -3.3V -> 5018; footprint TestPoint:TestPoint_THTPad_D2.0mm_Drill1.0mm -> SensEdu:5018
- TP5: value TX2 -> +1.25V; footprint TestPoint:TestPoint_THTPad_D2.0mm_Drill1.0mm -> SensEdu:TestPoint_THTPad_D2.0mm_Drill1.0mm
- TP6: value TX1 -> -3.3V; footprint TestPoint:TestPoint_THTPad_D2.0mm_Drill1.0mm -> SensEdu:TestPoint_THTPad_D2.0mm_Drill1.0mm
- U1: footprint SamacSys_Parts:SOT95P280X145-5N -> SensEdu:SOT95P280X145-5N
- U10: value DPS368XTSA1 -> SHT40-AD1F-R2; footprint SensEdu:DPS368XTSA1 -> SensEdu:SHT40AD1FR2
- U3: value SHT35-DIS-B2.5KS -> TS3312AQPR; footprint SensEdu:SHT35-DIS-B2.5KS -> SensEdu:TS3312AQPR; moved to B.Cu
- U8: value NC7SB3157P6X -> ADA4511-2ARMZ; footprint SensEdu:SOT65P210X110-6N -> SensEdu:SOP65P490X110-8N
- U9: value NC7SB3157P6X -> DPS368XTSA1; footprint SensEdu:SOT65P210X110-6N -> SensEdu:DPS368XTSA1; moved to F.Cu
- moved C18 48.3 mm to (165.8, 91.5)
- moved C3 42.3 mm to (113.4, 81.6), turned to 180 degrees
- moved C19 38.4 mm to (171.5, 55.2), turned to 90 degrees
- moved U3 35.9 mm to (116.5, 68.4), turned to 180 degrees
- moved C49 34.5 mm to (179.5, 82.6), turned to 0 degrees
- moved U9 32.8 mm to (149.9, 58.0), turned to 180 degrees
- moved C13 30.4 mm to (131.2, 61.2), turned to 180 degrees
- moved C12 30.2 mm to (131.2, 85.5), turned to 0 degrees
- moved C4 28.6 mm to (113.3, 84.6), turned to -90 degrees
- moved C1 27.5 mm to (113.0, 56.5), turned to 0 degrees
- moved C27 27.3 mm to (148.9, 76.4)
- moved C44 26.7 mm to (186.2, 86.7), turned to 90 degrees
- moved TP5 26.6 mm to (124.9, 65.5)
- moved C25 26.2 mm to (170.9, 60.4), turned to -90 degrees
- moved C16 26.2 mm to (128.8, 60.5), turned to -90 degrees
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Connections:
- net /*10 renamed /CS
- net /*11 renamed /COPI
- net /*12 renamed /CIPO
- net /*13 renamed /SCK
- net /*5 renamed /D5
- net /*8 renamed /SCL2
- net /*9 renamed /SDA2
- net /3* renamed /D2
- net /4* renamed /D3
- C1 pad 1: +3.3V -> /3V3_INO
- C10 pad 1: +3.3V -> +2.5V
- C11 pad 1: GND -> +2.5V
- C11 pad 2: +1.25V_REF -> GND
- C12 pad 1: +2.5V -> mic1_out_P
- C12 pad 2: GND -> mic1_out_N
- C13 pad 1: +2.5V -> mic2_out_P
- C13 pad 2: GND -> mic2_out_N
- C14 pad 1: mic1_out_P -> GND
- C15 pad 1: mic2_out_P -> GND
- C15 pad 2: mic2_out_N -> mic1_out_P
- C16 pad 2: mic1_out_N -> mic2_out_N
- C17 pad 2: mic1_out_P -> mic2_out_P
- C18 pad 1: GND -> +2.5V
- C18 pad 2: mic2_out_N -> GND
- C19 pad 1: GND -> +2.5V
- C19 pad 2: mic2_out_P -> GND
- C2 pad 1: /3V3_INO -> +2.5V
- C20 pad 1: +2.5V -> mic3_out_P
- C20 pad 2: GND -> mic3_out_N
- C21 pad 1: +2.5V -> mic4_out_P
- C21 pad 2: GND -> mic4_out_N
- C22 pad 1: mic3_out_P -> GND
- C23 pad 1: mic4_out_P -> GND
- C23 pad 2: mic4_out_N -> mic3_out_P
- C24 pad 2: mic3_out_N -> mic4_out_N
- C25 pad 2: mic3_out_P -> mic4_out_P
- C26 pad 1: GND -> +3.3V
- C26 pad 2: mic4_out_N -> GND
- C27 pad 1: GND -> +3.3V
- C27 pad 2: mic4_out_P -> GND
- C3 pad 1: +3.3V -> /Power/CP
- C34 pad 1: amp2_out_P -> amp1_out_P
- C34 pad 2: amp2_out_N -> amp1_out_N
- C35 pad 1: amp4_out_P -> amp2_out_P
- C35 pad 2: amp4_out_N -> amp2_out_N
- C37 pad 1: amp1_out_P -> amp4_out_P
- C37 pad 2: amp1_out_N -> amp4_out_N
- C38 pad 2: amp2_out_N -> amp1_out_N
- C39 pad 2: amp2_out_P -> amp1_out_P
- C4 pad 1: +2.5V -> /+5V_ARDUINO
- C40 pad 2: amp4_out_N -> amp2_out_N
- C41 pad 2: amp4_out_P -> amp2_out_P
- C44 pad 2: amp1_out_N -> amp4_out_N
- C45 pad 2: amp1_out_P -> amp4_out_P
- C48 pad 1: GND -> +3.3V
- C48 pad 2: +3.3V -> GND
- C49 pad 1: -3V3 -> +3.3V
- C5 pad 1: /Power/CP -> +3.3V
- C50 pad 1: -3V3 -> DAC1
- C50 pad 2: GND -> /Speakers/+IN_CH2
- C51 pad 1: GND -> -3V3
- C51 pad 2: +3.3V -> GND
- C52 pad 1: +3.3V -> -3V3
- C53 pad 1: /Speakers/SW1_OUT -> GND
- C53 pad 2: /Speakers/+IN_CH1 -> +3.3V
- C54 pad 1: /Speakers/TX1 -> +3.3V
- C54 pad 2: Net-(C54-Pad2) -> GND
- C55 pad 1: /Speakers/TX2 -> /Speakers/TX1
- C56 pad 1: GND -> /Speakers/TX2
- C56 pad 2: +3.3V -> Net-(C56-Pad2)
- C57 pad 1: /Speakers/SW2_OUT -> DAC0
- C57 pad 2: /Speakers/+IN_CH2 -> /Speakers/+IN_CH1
- C6 pad 1: /+5V_ARDUINO -> Net-(U2-C1+)
- C6 pad 2: GND -> Net-(U2-C1-)
- C7 pad 1: +3.3V -> GND
- C7 pad 2: GND -> -3V3
- C8 pad 1: Net-(U2-C1+) -> +3.3V
- C8 pad 2: Net-(U2-C1-) -> GND
- C9 pad 2: -3V3 -> +1.25V_REF
- J3 pad 6: unconnected-(J3-Pin_6-Pad6) -> /A5
- J3 pad 7: unconnected-(J3-Pin_7-Pad7) -> /A6
- J3 pad 8: unconnected-(J3-Pin_8-Pad8) -> /A7
- J4 pad 1: S2 -> /D7
- J4 pad 2: S1 -> /D6
- J4 pad 4: SE_PWM_1 -> /D4
- J7 pad 20: SE_PWM_2 -> unconnected-(J7-Pin_20-Pad20)
- J7 pad 7: SE_PWM_3 -> unconnected-(J7-Pin_7-Pad7)
- R30 pad 2: /Speakers/+IN_CH1 -> /Speakers/+IN_CH2
- R34 pad 2: Net-(C54-Pad2) -> Net-(C55-Pad2)
- R37 pad 2: Net-(C55-Pad2) -> Net-(C56-Pad2)
- R39 pad 2: /Speakers/+IN_CH2 -> /Speakers/+IN_CH1
- TP3 pad 1: +1.25V_REF -> GND
- TP4 pad 1: -3V3 -> GND
- TP5 pad 1: /Speakers/+IN_CH2 -> +1.25V_REF
- TP6 pad 1: /Speakers/+IN_CH1 -> -3V3
- U10 pad 1: GND -> /SDA
- U10 pad 2: unconnected-(U10-~{CSB}-Pad2) -> /SCL
- U10 pad 3: /SDA -> +3.3V
- U10 pad 4: /SCL -> GND
- U3 pad 1: /SDA -> unconnected-(U3-NC_1-Pad1)
- U3 pad 2: GND -> unconnected-(U3-NC_2-Pad2)
- U3 pad 4: /SCL -> GND
- U3 pad 7: GND -> unconnected-(U3-NC_5-Pad7)
- U3 pad 8: GND -> +1.25V_REF
- U8 pad 1: SE_PWM_1 -> /Speakers/TX1_IN
- U8 pad 2: GND -> /Speakers/-IN_CH1
- U8 pad 3: DAC1 -> /Speakers/+IN_CH1
- U8 pad 4: /Speakers/SW1_OUT -> -3V3
- U8 pad 5: +3.3V -> /Speakers/+IN_CH2
- U8 pad 6: S1 -> /Speakers/-IN_CH2
- U9 pad 1: SE_PWM_3 -> GND
- U9 pad 2: GND -> unconnected-(U9-~{CSB}-Pad2)
- U9 pad 3: DAC0 -> /SDA
- U9 pad 4: /Speakers/SW2_OUT -> /SCL
- U9 pad 5: +3.3V -> unconnected-(U9-SDO-Pad5)
- U9 pad 6: S2 -> +3.3V
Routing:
- net SE_PWM_1: track 73.8 -> 0.00 mm, vias 1 -> 0
- net SE_PWM_3: track 60.7 -> 0.00 mm, vias 1 -> 0
- net S1: track 53.8 -> 0.00 mm, vias 1 -> 0
- net S2: track 47.2 -> 0.00 mm, vias 1 -> 0
- net DAC1: track 30.5 -> 54.5 mm
- net /Speakers/+IN_CH1: track 19.2 -> 5.88 mm
- net GND: track 156.9 -> 144.6 mm, vias 60 -> 49
- net /Speakers/+IN_CH2: track 17.1 -> 5.89 mm
- net /Speakers/TX1: track 4.92 -> 15.7 mm
- net /SCL: track 58.5 -> 69.0 mm
- net /Speakers/TX2: track 7.88 -> 16.5 mm
- net +1.25V_REF: track 106.2 -> 102.1 mm
- net DAC0: track 36.4 -> 40.1 mm
- net /SDA: track 53.1 -> 50.3 mm
- net /Speakers/TX1_IN: track 27.1 -> 24.3 mm, vias 1 -> 2
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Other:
- board text added: "3.3V"
- board text added: "3.3V -> 1.25V"
- board text added: "Pin 1"
- board text added: "Vent hole"
- board text removed: "S1"
- board text removed: "S2"
